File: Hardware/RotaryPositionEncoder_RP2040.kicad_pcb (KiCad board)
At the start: 2 copper layers, 66 parts, among them J1 Conn_ABI, J2 Conn_UVW, J3 Conn_SWD, J4 USB_C_Receptacle_USB2.0, J5 Conn_5VDC, J6 Conn_CAN, U1 AS5047P, U2 RP2040, U3 M24C02-RMN, U4 W25Q32JVSS, U5 TJA1042T, U6 RT9013-33GB, Y1 Crystal_GND24

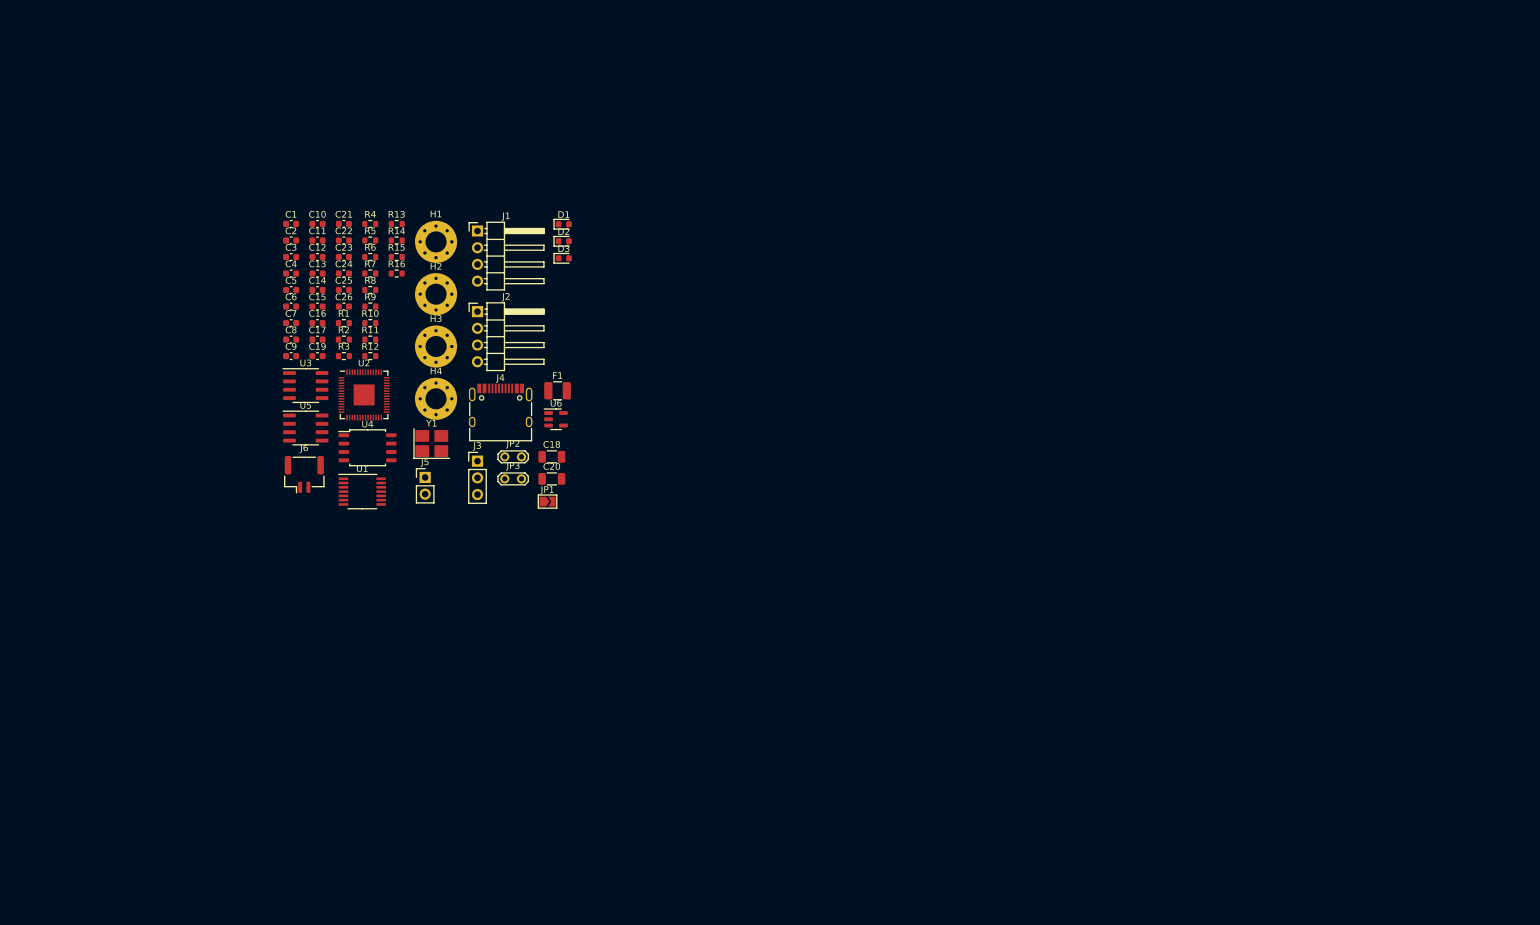
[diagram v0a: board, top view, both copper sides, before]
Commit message: sch modify pcb init
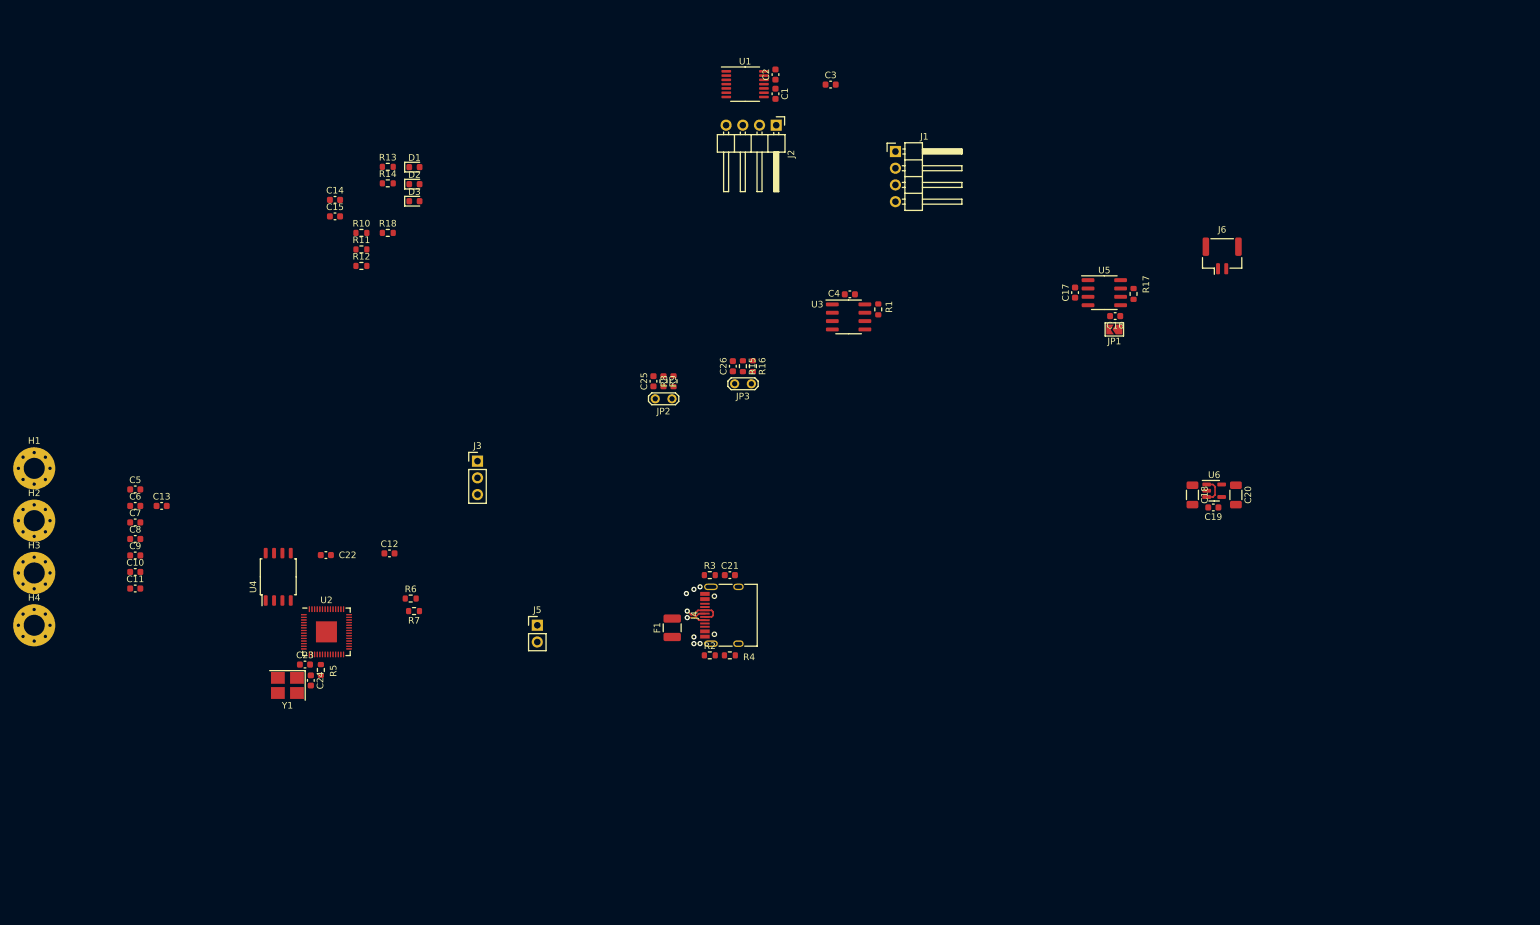
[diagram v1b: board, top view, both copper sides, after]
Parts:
- added R17: 120R, Resistor_SMD:R_0603_1608Metric, F.Cu at (211.5, 82.7)
- added R18: 33R, Resistor_SMD:R_0603_1608Metric, F.Cu at (98.2, 73.5)
- moved J6 143.4 mm to (225.0, 77.0)
- moved C19 138.1 mm to (223.6, 115.2), turned to 180 degrees
- moved U5 123.1 mm to (207.1, 82.5)
- moved C16 121.2 mm to (208.7, 86.1), turned to 180 degrees
- moved C17 115.3 mm to (202.6, 82.5), turned to 90 degrees
- moved C20 104.0 mm to (227.1, 113.3), turned to -90 degrees
- moved U6 100.6 mm to (223.8, 112.6)
- moved C18 97.5 mm to (220.5, 113.3), turned to -90 degrees
- moved JP1 90.0 mm to (208.6, 88.1), turned to 180 degrees
- moved C3 86.1 mm to (165.5, 50.9)
- moved R4 85.3 mm to (150.2, 137.7)
- moved C4 85.0 mm to (168.4, 82.8), turned to 180 degrees
- moved U1 85.0 mm to (152.5, 50.9)
- moved U3 83.2 mm to (168.2, 86.2)
- moved R1 81.2 mm to (172.7, 85.1), turned to 90 degrees
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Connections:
- net Net-(U2-VREG_VOUT) renamed /VREG
- R12 pad 2: Net-(U2-GPIO23) -> Net-(U2-GPIO8)
- R13 pad 2: Net-(U2-GPIO24) -> Net-(U2-GPIO9)
- R14 pad 2: Net-(U2-GPIO25) -> Net-(U2-GPIO10)
- R8 pad 1: /QSPI_SS -> Net-(JP2-B)
- R8 pad 2: Net-(JP2-B) -> /QSPI_SS
- U2 pad 11: unconnected-(U2-GPIO8-Pad11) -> Net-(U2-GPIO8)
- U2 pad 12: unconnected-(U2-GPIO9-Pad12) -> Net-(U2-GPIO9)
- U2 pad 13: unconnected-(U2-GPIO10-Pad13) -> Net-(U2-GPIO10)
- U2 pad 14: /SPI_MOSI -> unconnected-(U2-GPIO11-Pad14)
- U2 pad 15: /SPI_MISO -> unconnected-(U2-GPIO12-Pad15)
- U2 pad 16: /SPI_CS -> unconnected-(U2-GPIO13-Pad16)
- U2 pad 17: /SPI_CLK -> unconnected-(U2-GPIO14-Pad17)
- U2 pad 29: /CAN_TX -> unconnected-(U2-GPIO18-Pad29)
- U2 pad 30: /CAN_RX -> /SPI_MOSI
- U2 pad 31: unconnected-(U2-GPIO20-Pad31) -> /SPI_MISO
- U2 pad 32: unconnected-(U2-GPIO21-Pad32) -> /SPI_CS
- U2 pad 34: unconnected-(U2-GPIO22-Pad34) -> Net-(U2-GPIO22)
- U2 pad 35: Net-(U2-GPIO23) -> unconnected-(U2-GPIO23-Pad35)
- U2 pad 36: Net-(U2-GPIO24) -> /CAN_TX
- U2 pad 37: Net-(U2-GPIO25) -> /CAN_RX
- U2 pad 4: unconnected-(U2-GPIO2-Pad4) -> /I2C_SDA
- U2 pad 5: unconnected-(U2-GPIO3-Pad5) -> /I2C_SCL
- U2 pad 8: /I2C_SDA -> unconnected-(U2-GPIO6-Pad8)
- U2 pad 9: /I2C_SCL -> unconnected-(U2-GPIO7-Pad9)
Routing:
- net /USB_DP: track 0.00 -> 6.42 mm, vias 0 -> 1
- net /USB_DM: track 0.00 -> 4.65 mm, vias 0 -> 1
- net +5V: track 0.00 -> 4.05 mm
- net GND: vias 0 -> 6
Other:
- copper layers 2 -> 4

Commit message: add rs485
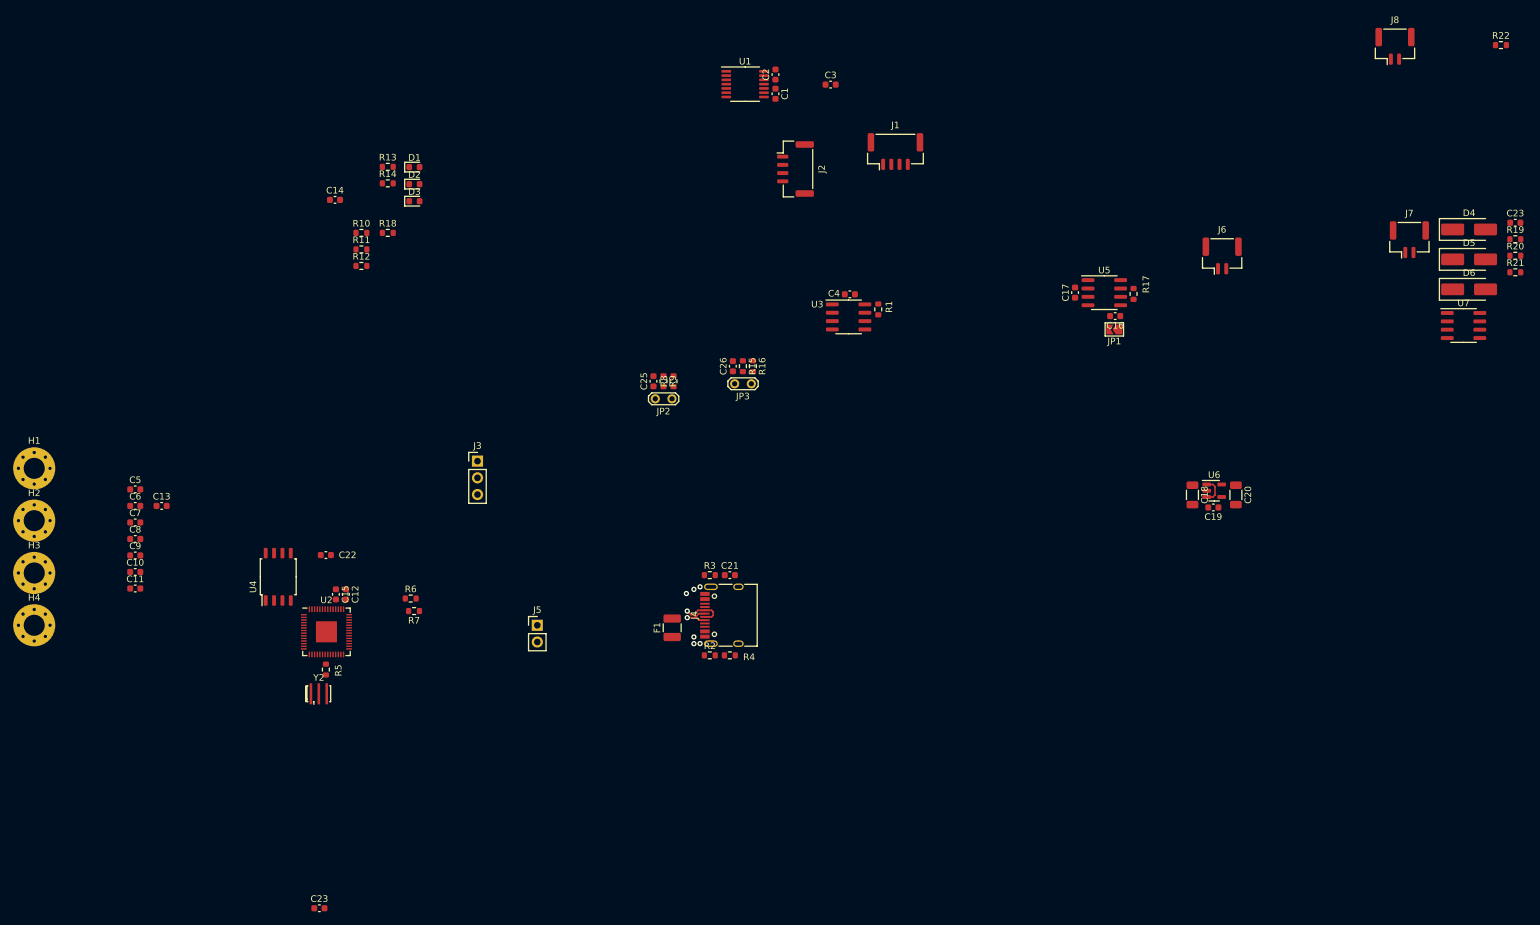
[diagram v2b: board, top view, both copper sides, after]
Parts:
- removed C24: 12pF, Capacitor_SMD:C_0603_1608Metric
- removed Y1: Crystal_GND24, Crystal:Crystal_SMD_3225-4Pin_3.2x2.5mm_HandSoldering
- added C23: 100nF, Capacitor_SMD:C_0603_1608Metric, F.Cu at (269.5, 71.9)
- added D4: TVS_5V, Diode_SMD:D_SMA_Handsoldering, F.Cu at (262.5, 72.9)
- added D5: TVS_5V, Diode_SMD:D_SMA_Handsoldering, F.Cu at (262.5, 77.5)
- added D6: TVS_5V, Diode_SMD:D_SMA_Handsoldering, F.Cu at (262.5, 82.0)
- added J7: Conn_CAN, Connector_JST:JST_GH_BM02B-GHS-TBT_1x02-1MP_P1.25mm_Vertical, F.Cu at (253.4, 74.5)
- added J8: Conn_CAN, Connector_JST:JST_GH_BM02B-GHS-TBT_1x02-1MP_P1.25mm_Vertical, F.Cu at (251.2, 45.1)
- added R19: 536R, Resistor_SMD:R_0603_1608Metric, F.Cu at (269.5, 74.4)
- added R20: 536R, Resistor_SMD:R_0603_1608Metric, F.Cu at (269.5, 76.9)
- added R21: 120R, Resistor_SMD:R_0603_1608Metric, F.Cu at (269.5, 79.5)
- added R22: 120R, Resistor_SMD:R_0603_1608Metric, F.Cu at (267.3, 44.9)
- added U7: MAX14783ExS, Package_SO:SOIC-8_3.9x4.9mm_P1.27mm, F.Cu at (261.7, 87.5)
- added Y2: Crystal_GND2, Crystal:Resonator_SMD_Murata_CSTxExxV-3Pin_3.0x1.1mm_HandSoldering, F.Cu at (87.7, 143.5)
- J1, J2: footprint Connector_PinHeader_2.54mm:PinHeader_1x04_P2.54mm_Horizontal -> Connector_JST:JST_GH_BM04B-GHS-TBT_1x04-1MP_P1.25mm_Vertical
- moved C15 57.4 mm to (90.3, 128.4), turned to -90 degrees
- moved C23 37.1 mm to (87.8, 176.1)
- moved C12 9.08 mm to (91.8, 128.4), turned to -90 degrees
- moved J2 7.28 mm to (160.1, 63.8)
- moved R5 0.76 mm to (88.8, 139.8)
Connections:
- U2 pad 15: unconnected-(U2-GPIO12-Pad15) -> /UART_TX
- U2 pad 16: unconnected-(U2-GPIO13-Pad16) -> /UART_RX
- U2 pad 18: unconnected-(U2-GPIO15-Pad18) -> /UART_RTS

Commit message: fix: CAN/RS485 connector footprint change: TVS -> NUP2105 change: Flash SOP->WSOP
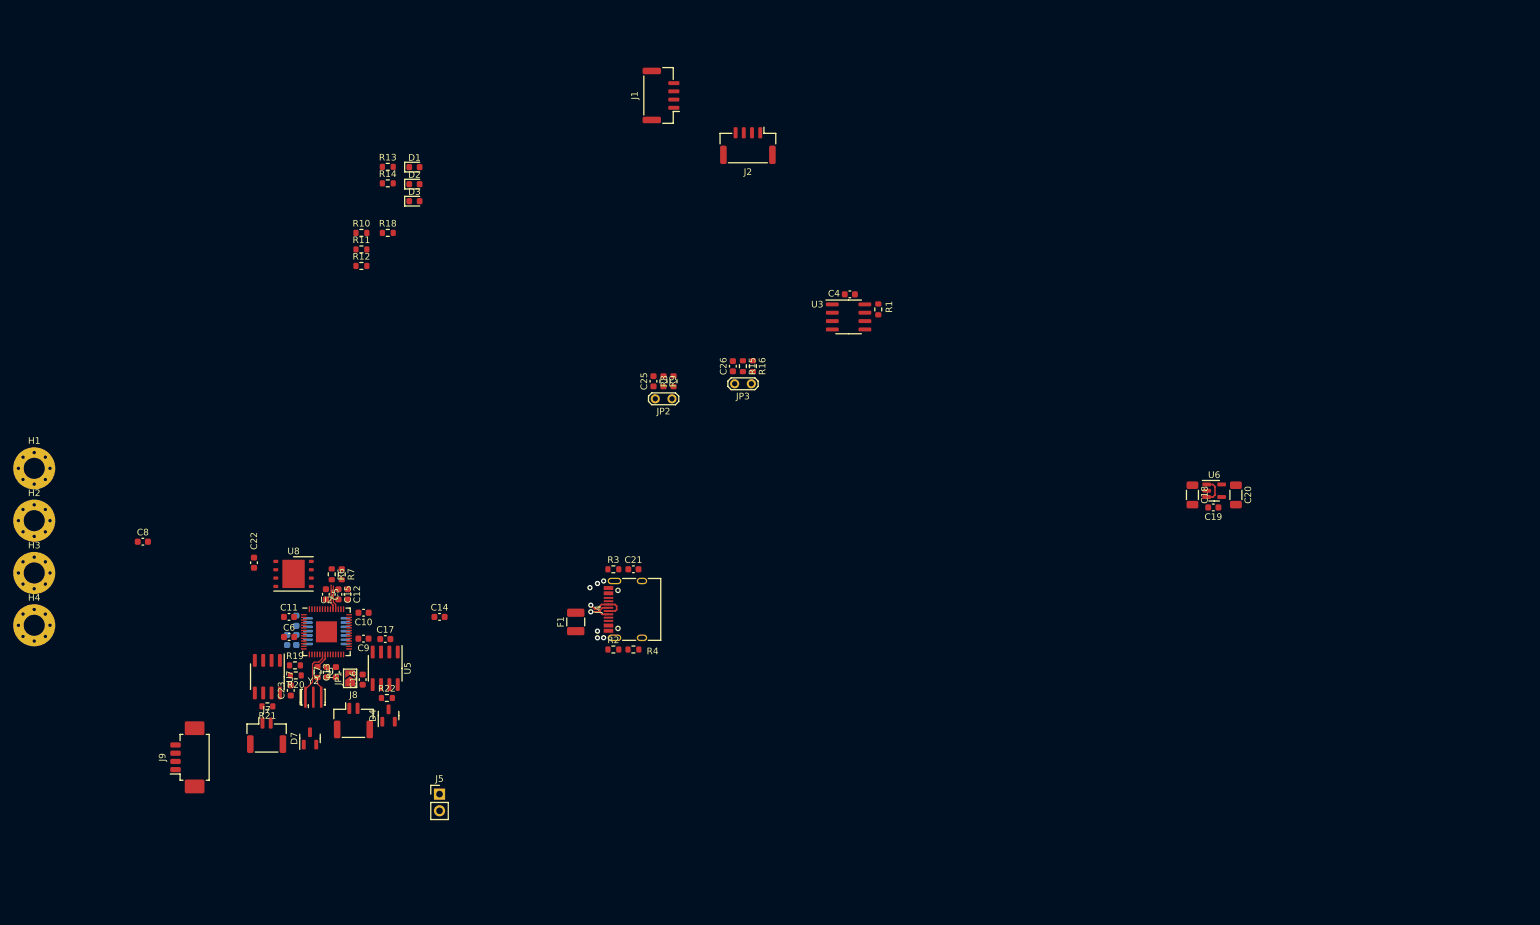
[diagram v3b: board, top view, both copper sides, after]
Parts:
- removed the C23 at (87.8, 176.1)
- removed D5, D6: TVS_5V, Diode_SMD:D_SMA_Handsoldering
- removed J3: Conn_SWD, Connector_PinHeader_2.54mm:PinHeader_1x03_P2.54mm_Vertical
- removed J6: Conn_CAN, Connector_JST:JST_GH_BM02B-GHS-TBT_1x02-1MP_P1.25mm_Vertical
- removed R17: 120R, Resistor_SMD:R_0603_1608Metric
- removed U4: W25Q32JVSS, Package_SO:SOIC-8_5.23x5.23mm_P1.27mm
- added D7: NUP2105L, Package_TO_SOT_SMD:SOT-23, F.Cu at (86.4, 150.3)
- added J9: Conn_01x04_MountingPin, Connector_Molex:Molex_PicoBlade_53261-0471_1x04-1MP_P1.25mm_Horizontal, F.Cu at (68.3, 153.2)
- added U8: W25Q32JVZP, Package_SON:WSON-8-1EP_6x5mm_P1.27mm_EP3.4x4.3mm, F.Cu at (83.9, 125.3)
- C1, C2, C3, U1: moved to B.Cu
- D4: value TVS_5V -> NUP2105L; footprint Diode_SMD:D_SMA_Handsoldering -> Package_TO_SOT_SMD:SOT-23
- J7, J8: footprint Connector_JST:JST_GH_BM02B-GHS-TBT_1x02-1MP_P1.25mm_Vertical -> Connector_JST:JST_GH_SM02B-GHS-TB_1x02-1MP_P1.25mm_Horizontal
- moved R21 200.8 mm to (79.9, 145.4), turned to 180 degrees
- moved C23 199.2 mm to (83.4, 143.0), turned to 90 degrees
- moved R19 196.4 mm to (84.1, 139.2)
- moved R22 196.2 mm to (98.0, 144.1)
- moved R20 196.0 mm to (84.2, 140.7), turned to 180 degrees
- moved U7 189.5 mm to (79.9, 140.9), turned to -90 degrees
- moved J7 189.3 mm to (79.8, 149.8)
- moved J8 188.6 mm to (93.0, 147.6)
- moved D4 180.1 mm to (98.3, 146.8), turned to 90 degrees
- moved JP1 127.7 mm to (92.5, 141.2), turned to 90 degrees
- moved C16 127.0 mm to (94.4, 141.4), turned to 90 degrees
- moved U5 123.3 mm to (97.8, 139.6), turned to -90 degrees
- moved C3 118.1 mm to (82.9, 135.3), turned to -90 degrees
- moved C17 117.3 mm to (97.8, 135.2), turned to 0 degrees
- moved C2 110.4 mm to (84.3, 132.4)
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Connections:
- D4 pad 1: GND -> /CAN_L
- D4 pad 2: /RS485_A -> /CAN_H
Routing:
- net Net-(U2-XIN): track 0.00 -> 7.95 mm
- net Net-(U2-USB_DP): track 0.00 -> 3.81 mm
- net Net-(U2-USB_DM): track 0.00 -> 3.67 mm
- net Net-(R5-Pad1): track 0.00 -> 3.22 mm
- net Net-(U2-XOUT): track 0.00 -> 2.34 mm

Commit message: Fix: RS485 Pullup/Pulldown Resistor
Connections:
- R19 pad 2: GND -> +5V
- R20 pad 1: +5V -> /RS485_B
- R20 pad 2: /RS485_B -> GND
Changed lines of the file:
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@@
       (net 49 "/RS485_A") (pintype "passive"))
     (pad "2" smd roundrect (at 0.825 0) (size 0.8 0.95) (layers "F.Cu" "F.Paste" "F.Mask") (roundrect_rratio 0.25)
-      (net 2 "GND") (pintype "passive"))
+      (net 1 "+5V") (pintype "passive"))
     (model "${KICAD6_3DMODEL_DIR}/Resistor_SMD.3dshapes/R_0603_1608Metric.wrl"
       (offset (xyz 0 0 0))
@@
       (stroke (width 0.1) (type solid)) (layer "F.Fab"))
     (pad "1" smd roundrect (at -0.825 0 180) (size 0.8 0.95) (layers "F.Cu" "F.Paste" "F.Mask") (roundrect_rratio 0.25)
-      (net 1 "+5V") (pintype "passive"))
+      (net 70 "/RS485_B") (pintype "passive"))
     (pad "2" smd roundrect (at 0.825 0 180) (size 0.8 0.95) (layers "F.Cu" "F.Paste" "F.Mask") (roundrect_rratio 0.25)
-      (net 70 "/RS485_B") (pintype "passive"))
+      (net 2 "GND") (pintype "passive"))
     (model "${KICAD6_3DMODEL_DIR}/Resistor_SMD.3dshapes/R_0603_1608Metric.wrl"
       (offset (xyz 0 0 0))
